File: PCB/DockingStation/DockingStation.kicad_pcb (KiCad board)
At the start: 4 copper layers, 147.2 x 63.2 mm, 256 parts, among them CN1 DSUB-15-HD_Socket_Horizontal_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, CN2 FDC_Connector, CN4 DSUB-25_Socket_Horizontal_P2.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, CN5 DSUB-9_Pins_Horizontal_P2.77x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, CN6 PS2 Connector, CN7 PS2 Connector, CN8 BarrelJack_Horizontal_PC110, J1 25-1MP_P0.5mm_Horizontal, J2 25-1MP_P0.5mm_Horizontal, J3 25-1MP_P0.5mm_Horizontal, J4 25-1MP_P0.5mm_Horizontal, Q1 3P4J, Q2 8C, U1 74VHCT244, U2 DNP (LT1237CS), U3 DS14C535MSA, U4 DNP

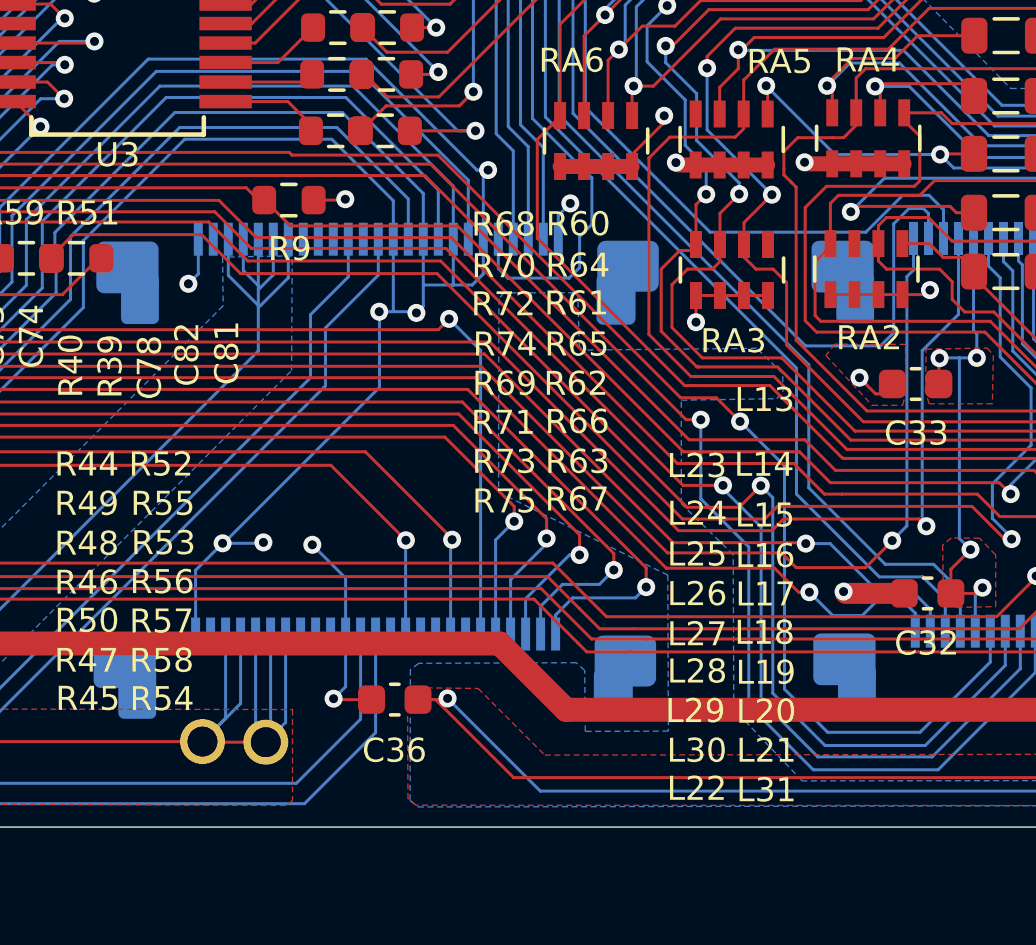
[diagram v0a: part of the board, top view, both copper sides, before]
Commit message: cleaned up dock board schematics
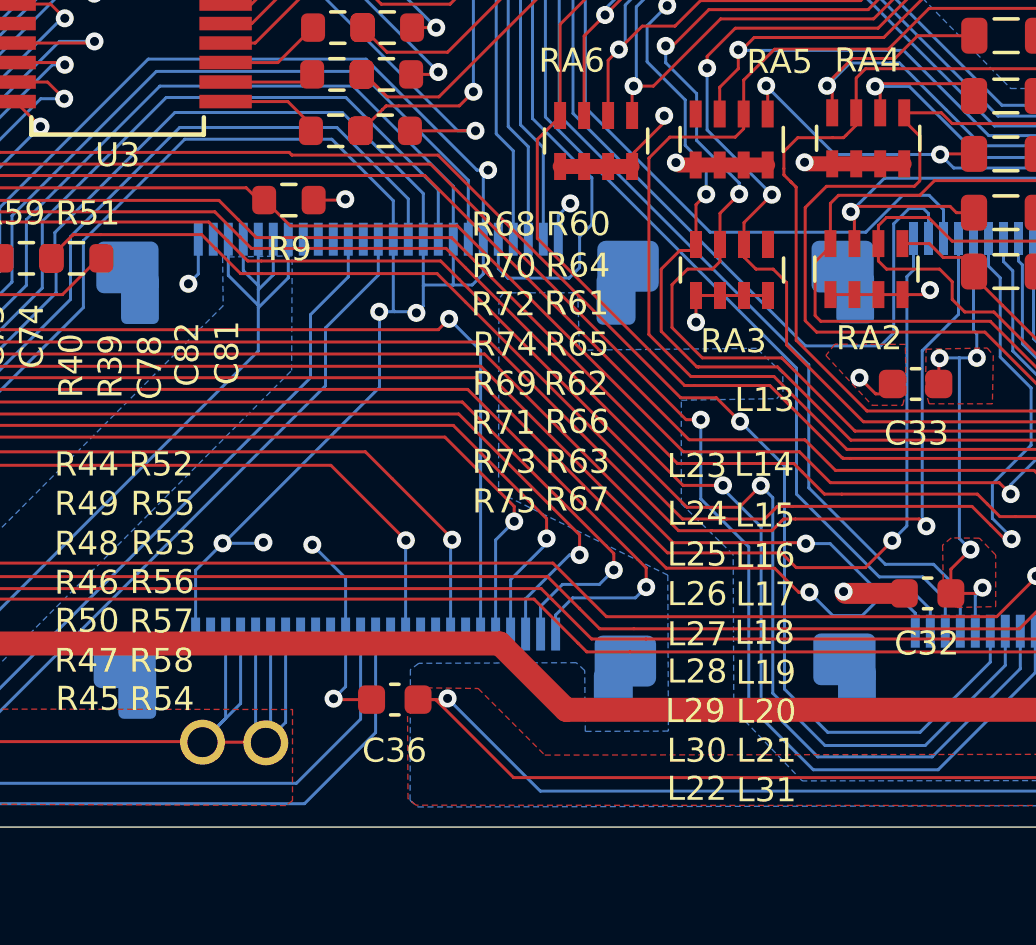
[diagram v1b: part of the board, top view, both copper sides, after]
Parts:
- removed the ? at (172.5, 115.6)
- removed the ? at (174.6, 115.6)
- added ?: , , F.Cu at (174.6, 115.6)
- added ?: , , F.Cu at (172.5, 115.6)
- C1, C33: value 330nF -> 0.22u
- C10, C2: value 1nF -> 1000p
- C11: value 2.5uF -> 2.2u
- C12, C15, C17, C19, C21, C23, C25, C27, C29: value 280nF -> 100p
- C13, C14, C16, C18, C20, C22, C24, C26, C28, C30: value 82pF -> 100p
- C3, C37, C38, C39, C4, C40, C41, C42, C43, C44, C63, C64, C65, C66: value 200pF -> 220p
- C31, C32, C34, C35, C36, C9: value 280nF -> 0.22u
- C45, C46, C47, C48, C49, C50, C51, C52, C53, C54, C55, C56, C57, C58, C59, C60, C61: value 200nF -> 220p
- C62, C67, C78: value 250nF -> 0.22u
- C68, C69, C70, C71, C72, C73, C74, C83, R10, R11, R29, R40, R42, R43, R44, R45, R46, R47, R48, R49, R50, R51, R60, R61, R62, R63, R64, R65, R66, R67, RA7, RA8, U4: value DNP -> ~
- C75: value 150nF -> 0.1u
- C76, C77: value 10nF -> 0.01u
- C79, C80, C81, C82: value 360nF -> 0.33u
- CN1: value DSUB-15-HD_Socket_Horizontal_P2.29x1.90mm_EdgePinOffset3.03mm_Housed_MountingHolesOffset4.94mm -> DZ11AAx
- CN2: value FDC_Connector -> 52629-2651
- CN4: value DSUB-25_Socket_Horizontal_P2.77x2.84mm_EdgePinOffset4.94mm_Housed_MountingHolesOffset4.94mm -> DZ113Ax
- CN5: value DSUB-9_Pins_Horizontal_P2.77x2.84mm_EdgePinOffset4.94mm_Housed_MountingHolesOffset4.94mm -> DZ101Ax
- CN6, CN7: value PS2 Connector -> TCS7927-56-401
- CN8: value BarrelJack_Horizontal_PC110 -> HEC3610-010020
- D2, D3: value s.3 5J -> EC15QS03L
- DA1, DA10, DA2, DA3, DA4, DA6, DA7, DA8: value 1W -> DCJ010
- DA11, DA12: value DNP -> 1
- DA9: value SOT-323_SC-70 -> ~
- F1: value 50v x1G0 JX30 -> RXE160
- J1, J2: value 25-1MP_P0.5mm_Horizontal -> 086212025340800
- J3, J4: value 25-1MP_P0.5mm_Horizontal -> 086210025340800
- L1, L2, L3: value 300nH -> ~
- L11, L13, L14, L15, L16, L17, L18, L19, L20, L21, L22, L23, L24, L25, L26, L27, L28, L29, L30, L31, L39, L40, L41, L42, L43, L44, L45, L46, L47, L48, L49, L5, L50, L51, L52, L53, L54, L55, L56, L57, L58, L59, L6, L60, L61, L62, L63, L64, L65, L66, L67: value 680nH -> 1.5u
- L34, L37, L38: value 300nH -> 560n
- L68: value EMI_Transformer -> ~
- Q1: value 3P4J -> 3P4J-ZK
- Q2: value 8C -> UN9213
- RA2, RA3, RA4: value 47k -> 4.7k
- SSFC1: value Fuse_2010_5025Metric -> ~
- U1: value 74VHCT244 -> TC74VHCT244FS
- U2: value DNP (LT1237CS) -> LT1237CS
- ZD1: value 18- -> MAZ8180-M
- ZD4: value 5_1 -> MAZ8051-L
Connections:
- net ACK# renamed Net-(C46-Pad2)
- net ACK#_L66 renamed Net-(L66-Pad1)
- net AUTOFD# renamed Net-(C52-Pad2)
- net AUTOFD#_L60 renamed Net-(L60-Pad1)
- net BLUE renamed Net-(CN1-Pad3)
- net BUSY renamed Net-(C45-Pad2)
- net BUSY_L67 renamed Net-(L67-Pad1)
- net CTS2# renamed Net-(C39-Pad1)
- net DA6 renamed Net-(DA10-C)
- net DA8_1 renamed Net-(DA7-C)
- net DA_2 renamed Net-(DA1-C)
- net DCD2# renamed Net-(C44-Pad1)
- net DSR2# renamed Net-(C43-Pad1)
- net DS_C1+ renamed Net-(U3-C1+)
- net DS_C1- renamed Net-(U3-C1-)
- net DS_C2+ renamed Net-(U3-C2+)
- net DS_C2- renamed Net-(U3-C2-)
- net DS_DIN1 renamed Net-(U3-DIN1)
- net DS_DIN2 renamed Net-(U3-DIN2)
- net DS_DIN3 renamed Net-(U3-DIN3)
- net DS_DOUT1 renamed Net-(U3-DOUT1)
- net DS_DOUT2 renamed Net-(U3-DOUT2)
- net DS_DOUT3 renamed Net-(U3-DOUT3)
- net DS_RIN1 renamed Net-(U3-RIN1)
- net DS_RIN2 renamed Net-(U3-RIN2)
- net DS_RIN3 renamed Net-(U3-RIN3)
- net DS_RIN4 renamed Net-(U3-RIN4)
- net DS_RIN5 renamed Net-(U3-RIN5)
- net DS_ROUT1 renamed Net-(U3-ROUT1)
- net DS_ROUT2 renamed Net-(U3-ROUT2)
- net DS_ROUT3 renamed Net-(U3-ROUT3)
- net DS_ROUT4 renamed Net-(U3-ROUT4)
- net DS_ROUT5 renamed Net-(U3-ROUT5)
- net DS_SHUTDN renamed Net-(U3-SHUTDOWN)
- net DS_V+ renamed Net-(U3-V+)
- net DS_V- renamed Net-(U3-V-)
- net DS_VCC renamed Net-(U3-VCC)
- net DTR2# renamed Net-(C38-Pad1)
- net ERROR# renamed Net-(C47-Pad2)
- net ERROR#_L65 renamed Net-(L65-Pad1)
- net FDC_ACK# renamed 1284_~{ACK}
- net FDC_AUTOFD# renamed 1284_~{AUTOFD}
- net FDC_BUSY renamed 1284_BUSY
- net FDC_CTS2# renamed 232_CTS
- net FDC_CTS2#_DS renamed Net-(L48-Pad1)
- net FDC_DCD2# renamed 232_DCD
- net FDC_DCD2#_DS renamed Net-(L43-Pad1)
- net FDC_DIR# renamed FDD_DIRSEL
- net FDC_DIR#_L17 renamed Net-(CN2-15)
- net FDC_DRATE0 renamed FDD_DRATE0
- net FDC_DRATE0_L25 renamed Net-(CN2-12)
- net FDC_DRATE1 renamed FDD_DRATE1
- net FDC_DRATE1_L13 renamed Net-(CN2-2)
- net FDC_DSKCHG# renamed FDD_DISKCHG
- net FDC_DSKCHG#_L22 renamed Net-(C12-Pad2)
- net FDC_DSR2# renamed 232_DSR
- net FDC_DSR2#_DS renamed Net-(L44-Pad1)
- net FDC_DTR2# renamed 232_DTR
- net FDC_DTR2#_DS renamed Net-(L49-Pad1)
- net FDC_ERROR# renamed 1284_~{FAULT}
- net FDC_HDSEL# renamed FDD_HEADSEL
- net FDC_HDSEL#_L21 renamed Net-(CN2-24)
- net FDC_INDEX# renamed FDD_INDEX
- net FDC_INDEX#_L14 renamed Net-(CN2-8)
- net FDC_INIT# renamed 1284_~{INIT}
- net FDC_PD0 renamed 1284_D1
- net FDC_PD1 renamed 1284_D2
- net FDC_PD2 renamed 1284_D3
- net FDC_PD3 renamed 1284_D4
- net FDC_PD4 renamed 1284_D5
- net FDC_PD5 renamed 1284_D6
- net FDC_PD6 renamed 1284_D7
- net FDC_PD6_R21 renamed Net-(L52-Pad1)
- net FDC_PD7 renamed 1284_D8
- net FDC_PE renamed 1284_PERROR
- net FDC_RDATA#_L30 renamed Net-(CN2-23)
- net FDC_RI2# renamed 232_RI
- net FDC_RI2#_DS renamed Net-(L50-Pad1)
- net FDC_RTS2# renamed 232_RTS
- net FDC_RTS2#_DS renamed Net-(L46-Pad1)
- net FDC_RX_DS renamed Net-(L45-Pad1)
- net FDC_SLCT renamed 1284_SELECT
- net FDC_SLCTIN# renamed 1284_~{SELECTIN}
- net FDC_STEP# renamed FDD_STEP
- net FDC_STEP#_L27 renamed Net-(CN2-16)
- net FDC_STROBE# renamed 1284_~{STROBE}
- net FDC_TRK0 renamed FDD_TRK00
- net FDC_TRK0_L19 renamed Net-(CN2-20)
- net FDC_TX_DS renamed Net-(L47-Pad1)
- net FDC_WDATA# renamed FDD_WDATA
- net FDC_WDATA#_L18 renamed Net-(CN2-17)
- net FDC_WGATE# renamed FDD_WGATE
- net FDC_WGATE#_L28 renamed Net-(CN2-18)
- net FDC_WRTPRT# renamed FDD_WPRT
- net FDC_WRTPRT#_L20 renamed Net-(CN2-22)
- net FDD_Bowman renamed FDD_DETFDD
- net FDD_Bowman_L31 renamed Net-(CN2-25)
- net FDD_DRSEL renamed FDD_DRVSEL
- net FDD_DRSEL_L16 renamed Net-(CN2-11)
- net FDD_MOTEN renamed FDD_MOTON
- net FDD_MOTEN_L16 renamed Net-(CN2-13)
- net FDD_PWR renamed +5V_FDD
- net FDD_PWR_L11 renamed Net-(CN2-10)
- net FDD_Pluto1 renamed FDD_PLUTO1
- net FDD_Pluto1_L23 renamed Net-(CN2-4)
- net FDD_Pluto2 renamed FDD_PLUTO2
- net FDD_Pluto2_L24 renamed Net-(CN2-9)
- net FDD_Pluto3 renamed FDD_PLUTO3
- net FDD_Pluto3_L26 renamed Net-(CN2-14)
- net FDD_Pluto4 renamed FDD_PLUTO4
- net FDD_Pluto4_L29 renamed Net-(CN2-21)
- net GREEN renamed Net-(CN1-Pad2)
- net HSync renamed Net-(C3-Pad1)
- net HSync_R2 renamed Net-(L6-Pad1)
- net Hsync_Buffered renamed Net-(U1-2Y1)
- net INIT# renamed Net-(C51-Pad2)
- net INIT#_L61 renamed Net-(L61-Pad1)
- net J13_79_PC110 renamed 232_EN
- net KB_INT1 renamed PS2_1_DATA
- net KB_INT1_PS2 renamed Net-(C66-Pad2)
- net KB_INT2 renamed PS2_1_CLOCK
- net KB_INT2_PS2 renamed Net-(C65-Pad2)
- net KB_INT3 renamed PS2_2_CLOCK
- net KB_INT3_PS2 renamed Net-(C63-Pad2)
- net KB_INT4 renamed PS2_2_DATA
- net KB_INT4_PS2 renamed Net-(C64-Pad2)
- net L37_2 renamed Net-(C62-Pad1)
- net LT_C1+ renamed Net-(U2-C1+)
- net LT_C1- renamed Net-(U2-C1-)
- net LT_C2+ renamed Net-(U2-C2-)
- net LT_C2- renamed Net-(U2-C2+)
- net LT_DR1_IN renamed Net-(U2-DR1IN)
- net LT_DR1_OUT renamed Net-(U2-DR1OUT)
- net LT_DR2_IN renamed Net-(U2-DR2IN)
- net LT_DR2_OUT renamed Net-(U2-DR2OUT)
- net LT_DR3_IN renamed Net-(U2-DR3IN)
- net LT_DR3_OUT renamed Net-(U2-DR3OUT)
- net LT_DRIVER_DISABLE renamed Net-(U2-DRIVER_DISABLE)
- net LT_ON_OFF renamed Net-(U2-ON/OFF)
- net LT_RX1_IN renamed Net-(U2-RX1IN)
- net LT_RX1_OUT renamed Net-(U2-RX1OUT)
- net LT_RX2_IN renamed Net-(U2-RX2IN)
- net LT_RX2_OUT renamed Net-(U2-RX2OUT)
- net LT_RX3_IN renamed Net-(U2-RX3IN)
- net LT_RX3_OUT renamed Net-(U2-RX3OUT)
- net LT_RX4_IN renamed Net-(U2-RX4IN)
- net LT_RX4_OUT renamed Net-(U2-RX4OUT)
- net LT_RX5_IN renamed Net-(U2-RX5IN)
- net LT_RX5_OUT renamed Net-(U2-RX5OUT)
- net LT_V+ renamed Net-(U2-V+)
- net LT_V- renamed Net-(U2-V-)
- net LT_VCC renamed Net-(U2-VCC)
- net M38_P46_P34 renamed VIN_AC_DET
- net M38_P67 renamed VIN_AC_DET_DIV
- net PD0 renamed Net-(C54-Pad2)
- net PD0_L58 renamed Net-(L58-Pad1)
- net PD1 renamed Net-(C55-Pad2)
- net PD1_L57 renamed Net-(L57-Pad1)
- net PD2 renamed Net-(C56-Pad2)
- net PD2_L56 renamed Net-(L56-Pad1)
- net PD3 renamed Net-(C57-Pad2)
- net PD3_L55 renamed Net-(L55-Pad1)
- net PD4 renamed Net-(C58-Pad2)
- net PD4_L54 renamed Net-(L54-Pad1)
- net PD5 renamed Net-(C59-Pad2)
- net PD5_L53 renamed Net-(L53-Pad1)
- net PD6 renamed Net-(C60-Pad2)
- net PD7 renamed Net-(C61-Pad2)
- net PD7_L51 renamed Net-(L51-Pad1)
- net PE renamed Net-(C48-Pad2)
- net PE_L64 renamed Net-(L64-Pad1)
- net PNET2 renamed +5V_VGA
- net PNET5 renamed +5V_232
- net PNET5_Q1_F2 renamed +5V_PS2
- net PWR_IN+ renamed Net-(C76-Pad2)
- net PWR_IN+_Diode renamed VIN_AC
- net PWR_IN+_EMI renamed Net-(C77-Pad1)
- net PWR_IN+_Fuse renamed Net-(D2-A)
- net PWR_IN- renamed Net-(C76-Pad1)
- net PWR_IN-_EMI renamed GND_VIN_AC
- net Pluto_Dock1_PC110 renamed Net-(J3-Pad2)
- net Pluto_Dock2_PC110 renamed Net-(J2-Pad2)
- net Q1_3 renamed Net-(Q1-G)
- net Q2_1 renamed Net-(Q2-B)
- net R269_1_PC110 renamed VIN_AC_LP
- net R30_2 renamed Net-(ZD1-A)
- net R33_2 renamed Net-(R32-Pad1)
- net R37_2 renamed Net-(R36-Pad1)
- net R5_2 renamed Net-(DA8-C)
- net RA7 renamed Net-(DA12-C)
- net RA8 renamed Net-(DA11-C)
- net RED renamed Net-(CN1-Pad1)
- net RI2# renamed Net-(C37-Pad1)
- net RTS2# renamed Net-(C41-Pad1)
- net RX renamed Net-(C42-Pad2)
- net SLCT renamed Net-(C49-Pad2)
- net SLCTIN# renamed Net-(C50-Pad2)
- net SLCTIN#_L62 renamed Net-(L62-Pad1)
- net SLCT_L63 renamed Net-(L63-Pad1)
- net STROBE# renamed Net-(C53-Pad2)
- net STROBE#_L59 renamed Net-(L59-Pad1)
- net TX renamed Net-(C40-Pad1)
- net U29_A2_FDC_IRRX_RXD2 renamed 232_RXD
- net U29_Y1_FDC_IRTX_TXD2 renamed 232_TXD
- net U4_2 renamed Net-(U4A-I)
- net U4_5 renamed Net-(U4B-VCC)
- net VCC2_PS2 renamed Net-(CN7-Pad4)
- net VCC_PS2 renamed Net-(CN6-Pad4)
- net VGA_Hsync renamed VGA_HSYNC
- net VGA_Hsync_R3 renamed Net-(DA6-CA)
- net VGA_Vsync renamed VGA_VSYNC
- net VGA_Vsync_R4 renamed Net-(DA10-CA)
- net VSync renamed Net-(C4-Pad1)
- net VSync_R1 renamed Net-(L5-Pad1)
- net Vsync_Buffered renamed Net-(U1-1Y1)
- CN1 pad 10: CN1_10 -> GND
- CN1 pad 11: CN1_11 -> unconnected-(CN1-Pad11)
- CN1 pad 12: CN1_12 -> unconnected-(CN1-Pad12)
- CN1 pad 15: CN1_15 -> unconnected-(CN1-Pad15)
- CN1 pad 4: CN1_4 -> unconnected-(CN1-Pad4)
- CN1 pad 9: CN1_9 -> unconnected-(CN1-Pad9)
- CN2 pad 16: CN2_6 -> unconnected-(CN2-6-Pad16)
- CN7 pad 2: CN7_2 -> unconnected-(CN7-Pad2)
- CN7 pad 6: CN7_6 -> unconnected-(CN7-Pad6)
- DA4 pad 3: DA4_3 -> unconnected-(DA4-CA-Pad3)
- DA7 pad 3: DA7_3 -> unconnected-(DA7-CA-Pad3)
- DA8 pad 3: DA8_3 -> unconnected-(DA8-CA-Pad3)
- DA9 pad 3: DA9_3 -> unconnected-(DA9-CA-Pad3)
- J1 pad 14: M38_P16_R80_PC110 -> unconnected-(J1-Pad14)
- J1 pad 16: MN195_IRQ1# -> unconnected-(J1-Pad16)
- J1 pad 17: MN195_ADCK# -> unconnected-(J1-Pad17)
- J1 pad 18: MN195_S11_BUF -> unconnected-(J1-Pad18)
- J1 pad 24: MN192_VPDA# -> unconnected-(J1-Pad24)
- J1 pad MP: (no net) -> unconnected-(J1-PadMP)_1
- J2 pad 10: FDC_RDATA# -> FDD_RDATA
- J2 pad MP: (no net) -> unconnected-(J2-PadMP)_1
- J3 pad MP: (no net) -> unconnected-(J3-PadMP)_3
- J4 pad 10: J13_35_PC110 -> unconnected-(J4-Pad10)
- J4 pad 12: J13_37_PC110 -> unconnected-(J4-Pad12)
- J4 pad 16: Modem_RSRVD2 -> unconnected-(J4-Pad16)
- J4 pad 17: Modem_RSRVD1 -> unconnected-(J4-Pad17)
- J4 pad 18: J13_43_PC110 -> unconnected-(J4-Pad18)
- J4 pad 24: J13_49_PC110 -> unconnected-(J4-Pad24)
- J4 pad 7: J13_32_PC110 -> unconnected-(J4-Pad7)
- J4 pad 9: J13_34_PC110 -> unconnected-(J4-Pad9)
- J4 pad MP: (no net) -> unconnected-(J4-PadMP)_2
- L30 pad 1: FDC_RDATA# -> FDD_RDATA
- RA2 pad 7: RA2_7 -> FDD_RDATA
- RA3 pad 5: RA3_5 -> unconnected-(RA3-Pad5)
- RA5 pad 8: RA5_8 -> unconnected-(RA5-Pad8)
- U2 pad 14: LT_NC1 -> (no net)
- U2 pad 15: LT_NC2 -> (no net)
- U3 pad 24: DS_NC2 -> (no net)
- U3 pad 6: DS_NC1 -> (no net)
- U4 pad 1: U4_1 -> (no net)
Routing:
- net FDD_RDATA: track 0.00 -> 16.9 mm, vias 0 -> 1
- net FDC_RDATA#: track 15.8 -> 0.00 mm, vias 1 -> 0
- net GND: track 1285.3 -> 1299.4 mm, vias 114 -> 117
- net PIN: track 14.0 -> 0.00 mm, vias 3 -> 0
- removed copper zone on F.Cu, net PIN
